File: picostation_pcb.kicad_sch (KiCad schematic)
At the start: 69 parts, among them J1 USB_C_Receptacle_USB2.0, J2 +, J3 D, J4 C, J5 G, J6 Conn_01x20, SW1 BOOT, U1 LM78M05_TO252, U3 RP2040, U4 W25Q16JVSSIQ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

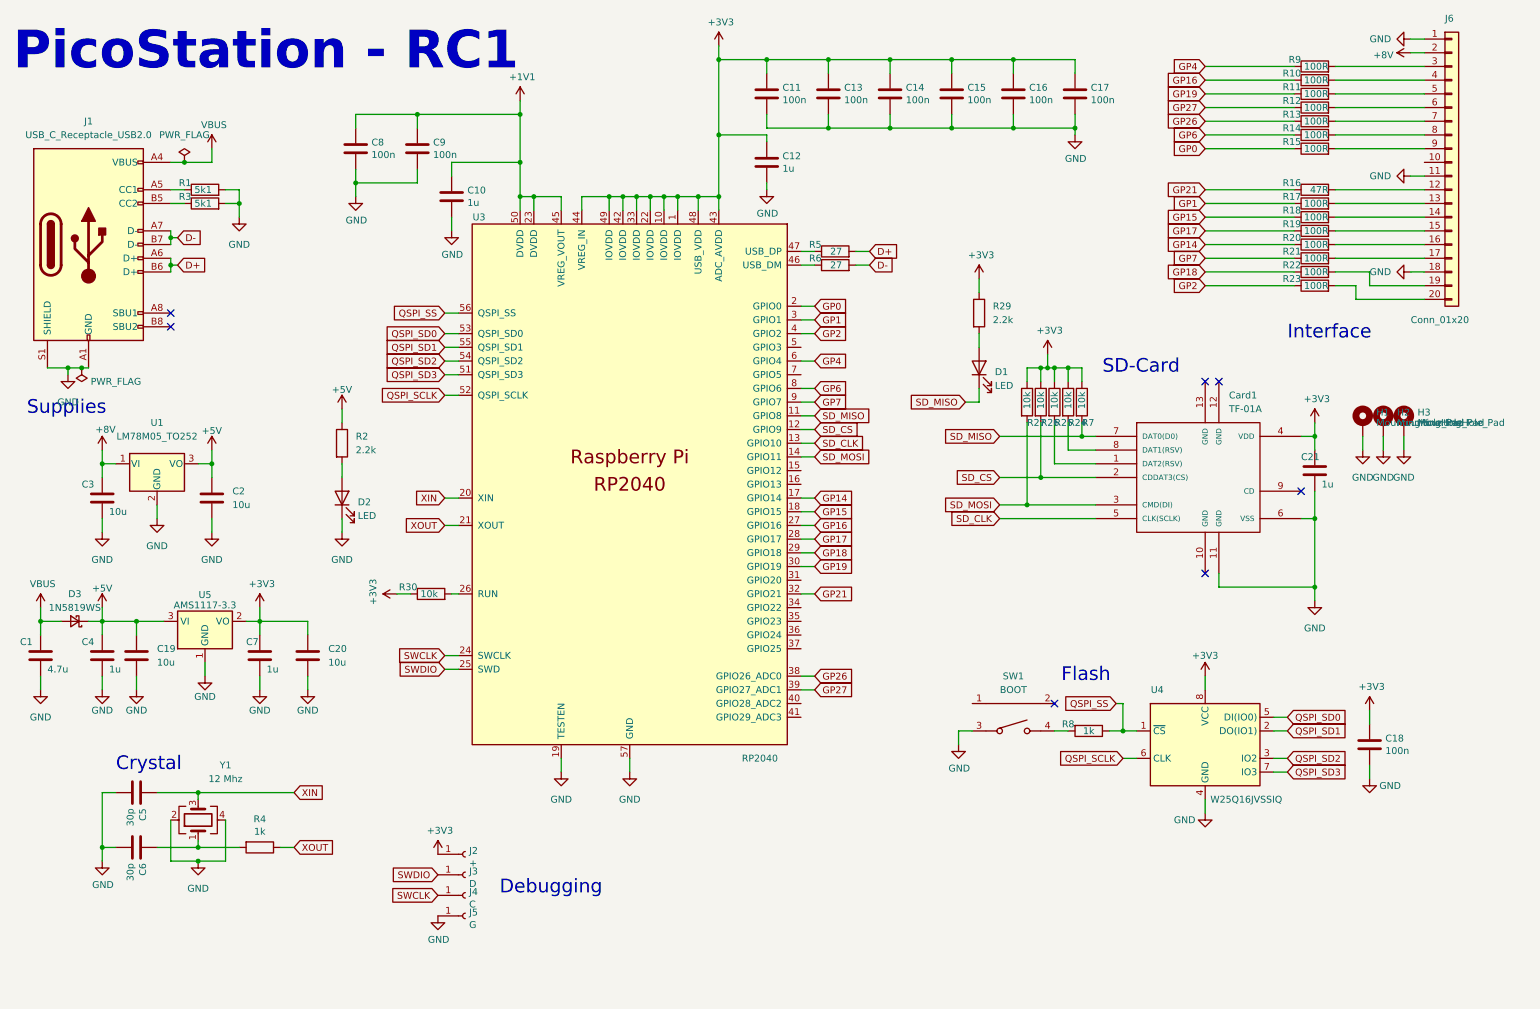
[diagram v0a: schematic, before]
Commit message: Small PCB Improvements
Ordered a fully assembled board from JLCPCB, tested it for 5+ hours
while playing the fan translation of Policenauts. Tested several
other games as well for a short period of time (Silent Hill, Crash
Bandicoot, Spyro)

- Remove 5V 7805 regulator, diode OR the power from the 8V line into the
  AMS1117-3v3 instead (this part can accept up to 18V)
- Add a debug header that is compatible with the Raspberry Pi Debug
  Probe
- Add a reset switch
- Update photos
- Replace 2.2k resistors with 1k to improve ease of manufacturing
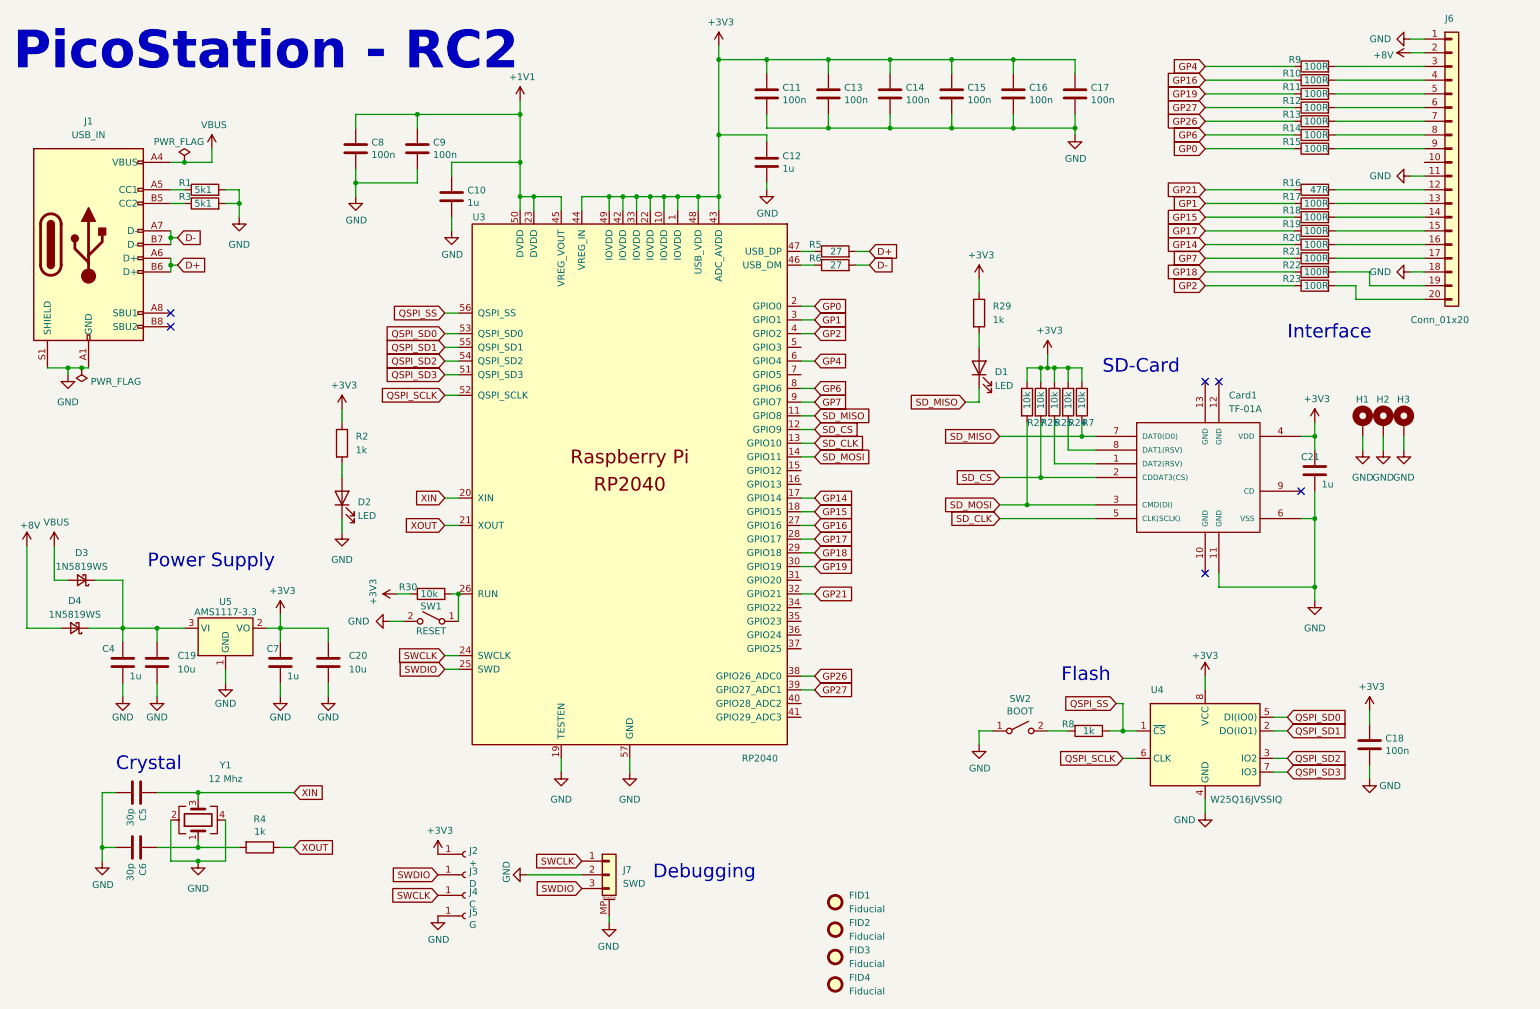
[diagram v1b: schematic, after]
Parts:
- removed C1: 4.7u, Capacitor_SMD:C_0603_1608Metric_Pad1.08x0.95mm_HandSolder, symbol Device:C
- removed C2, C3: 10u, Capacitor_SMD:C_0805_2012Metric_Pad1.18x1.45mm_HandSolder, symbol Device:C
- removed SW1: BOOT, kicad_lceda:SW-SMD_TS24CA, symbol kicad_lceda:TS24CA
- removed U1: LM78M05_TO252, Package_TO_SOT_SMD:TO-252-2, symbol Regulator_Linear:LM78M05_TO252
- added D4: 1N5819WS, Diode_SMD:D_SOD-323, symbol Device:D_Schottky_Small
- added FID1, FID2, FID3, FID4: Fiducial, Fiducial:Fiducial_1mm_Mask2mm, symbol Mechanical:Fiducial
- added J7: SWD, Connector_JST:JST_SH_BM03B-SRSS-TB_1x03-1MP_P1.00mm_Vertical, symbol Connector_Generic_MountingPin:Conn_01x03_MountingPin
- added SW1: RESET, Button_Switch_SMD:SW_SPST_EVPBF, symbol Switch:SW_SPST
- added SW2: BOOT, Button_Switch_SMD:SW_SPST_EVPBF, symbol Switch:SW_SPST
- H1, H2, H3: value MountingHole_Pad -> ~
- J1: value USB_C_Receptacle_USB2.0 -> USB_IN
- R2, R29: value 2.2k -> 1k
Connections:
- net +3V3: now also R2.1
- net +8V: now also D4.2 (A)
- net GND: now also J7.2 (Pin_2), J7.MP (MountPin), SW1.2 (B), SW2.1 (A)
- net SWCLK: now also J7.1 (Pin_1)
- net SWDIO: now also J7.3 (Pin_3)
- net at R8.2: now also SW2.2 (B)
- net at R30.2, U3.26 (RUN): now also SW1.1 (A)
- net +5V: no longer names the net of C19.1, C4.1, D3.1 (K), U5.3 (VI)
- net +5V: now also D4.1 (K); no longer R2.1
- no-connect marks 7 -> 6
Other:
- note added: "PicoStation - RC2"
- note added: "Power Supply"
- note removed: "PicoStation - RC1"
- note removed: "Supplies"
- moved on the sheet: C19, C20, C4, C7, D3, U5
